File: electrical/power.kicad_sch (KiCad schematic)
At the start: 72 parts

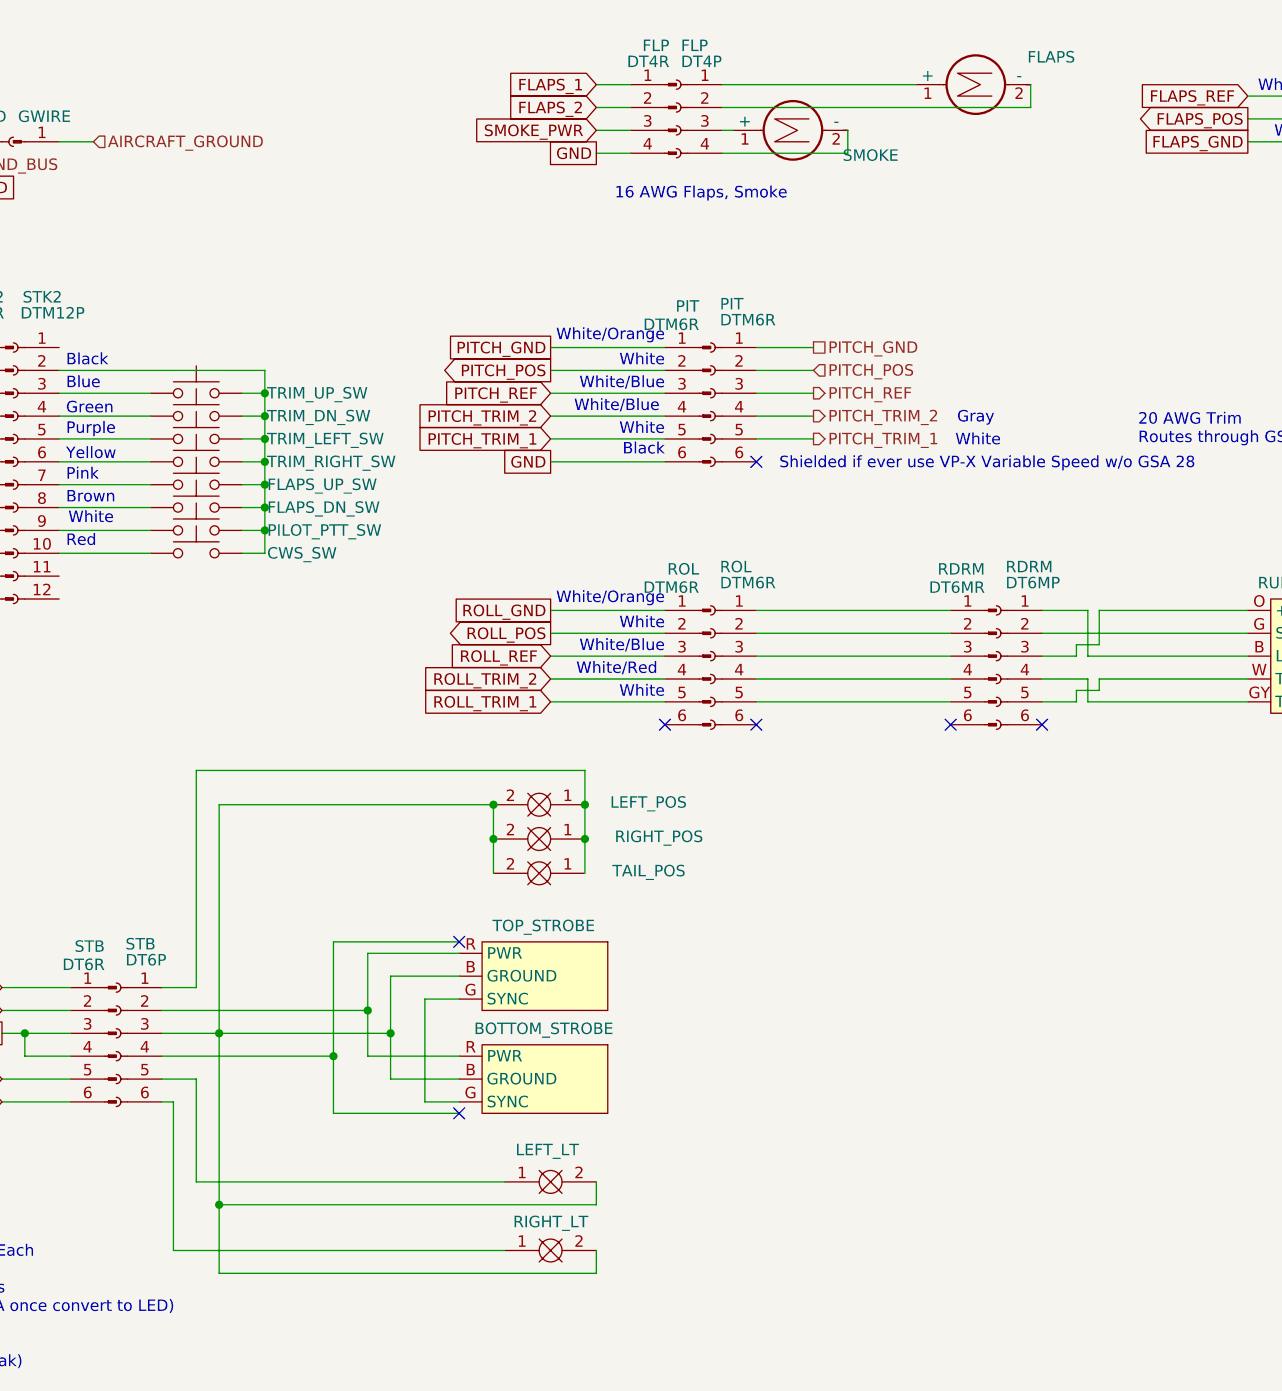
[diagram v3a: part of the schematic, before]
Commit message: Interim check-in getting colors correct.
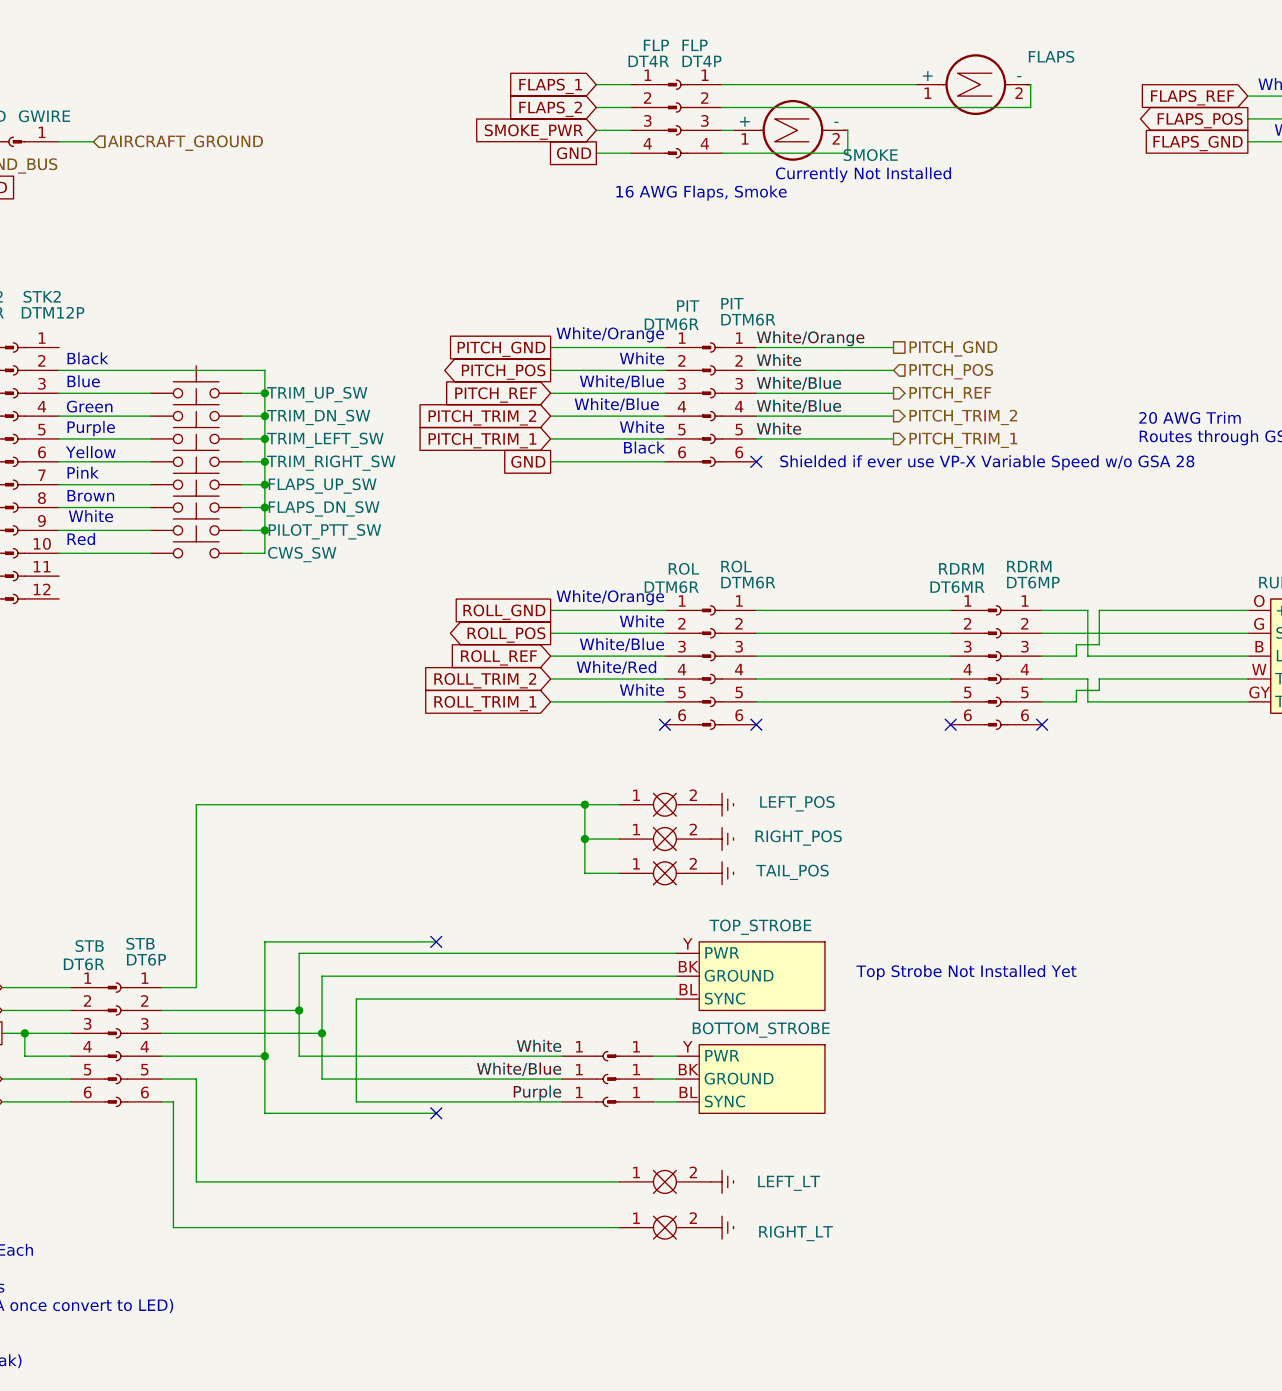
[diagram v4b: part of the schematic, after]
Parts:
- added J1, J4, J5: Conn_01x01_Pin, symbol Connector:Conn_01x01_Pin
- added J2, J3, J6: Conn_01x01_Socket, symbol Connector:Conn_01x01_Socket
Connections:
- net PITCH_TRIM_1 is gone; now on net PITCH_POS: PIT.5 (Pin_5), PIT.5 (Pin_5), VPX.J1_11 (PITCH_TRIM_MOTOR)
- net PITCH_TRIM_2 is gone; now on net PITCH_REF: PIT.4 (Pin_4), PIT.4 (Pin_4), VPX.J1_12 (PITCH_TRIM_MOTOR)
- net PITCH_POS: now also STB.2 (Pin_2), TOP_STROBE.Y (PWR), J2.1 (Pin_1)
- net PITCH_REF: now also STB.3 (Pin_3), TOP_STROBE.BK (GROUND), J3.1 (Pin_1)
- net Earth: now reaches LEFT_LT.2, LEFT_POS.2, RIGHT_LT.2, RIGHT_POS.2, TAIL_POS.2
- net Earth: no longer BOTTOM_STROBE.B (GROUND), STB.3 (Pin_3), TOP_STROBE.B (GROUND)
- new net: BOTTOM_STROBE.BK (GROUND), J4.1 (Pin_1)
- new net: BOTTOM_STROBE.BL (SYNC), J5.1 (Pin_1)
- new net: BOTTOM_STROBE.Y (PWR), J1.1 (Pin_1)
- new net Purple: J6.1 (Pin_1), TOP_STROBE.BL (SYNC)
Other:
- note added: "Currently Not Installed"
- note added: "Top Strobe Not Installed Yet"
- moved on the sheet: BOTTOM_STROBE, LEFT_LT, LEFT_POS, RIGHT_LT, RIGHT_POS, TAIL_POS, TOP_STROBE

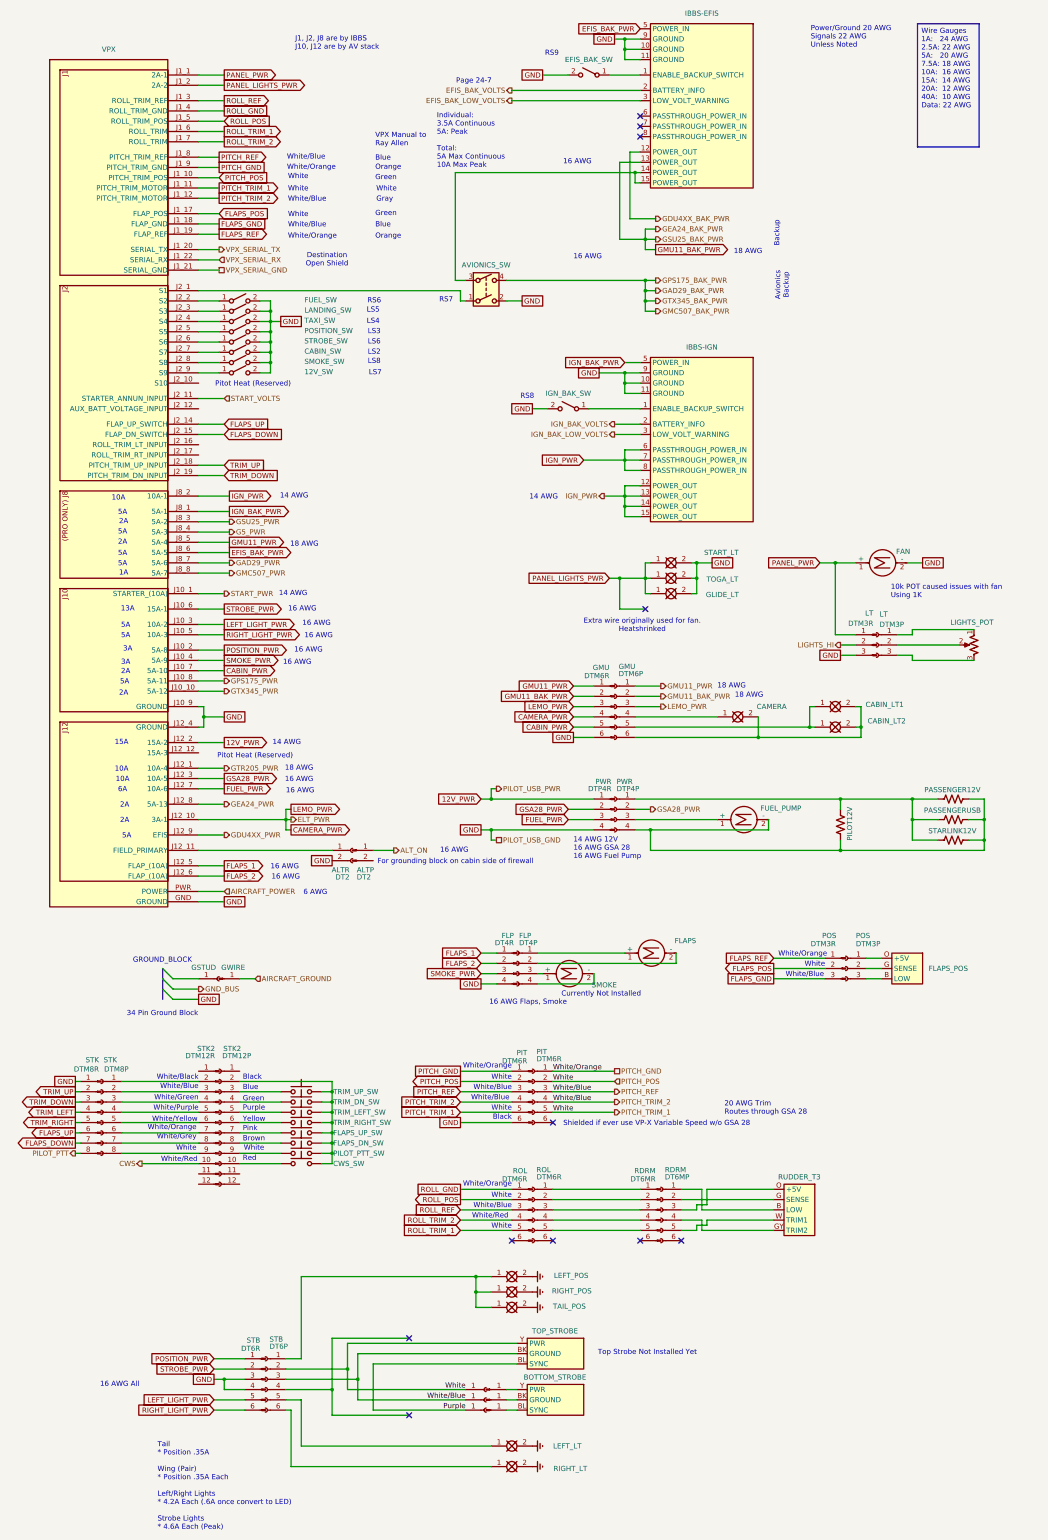
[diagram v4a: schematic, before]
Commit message: Added shielding and wire colors and corrections.
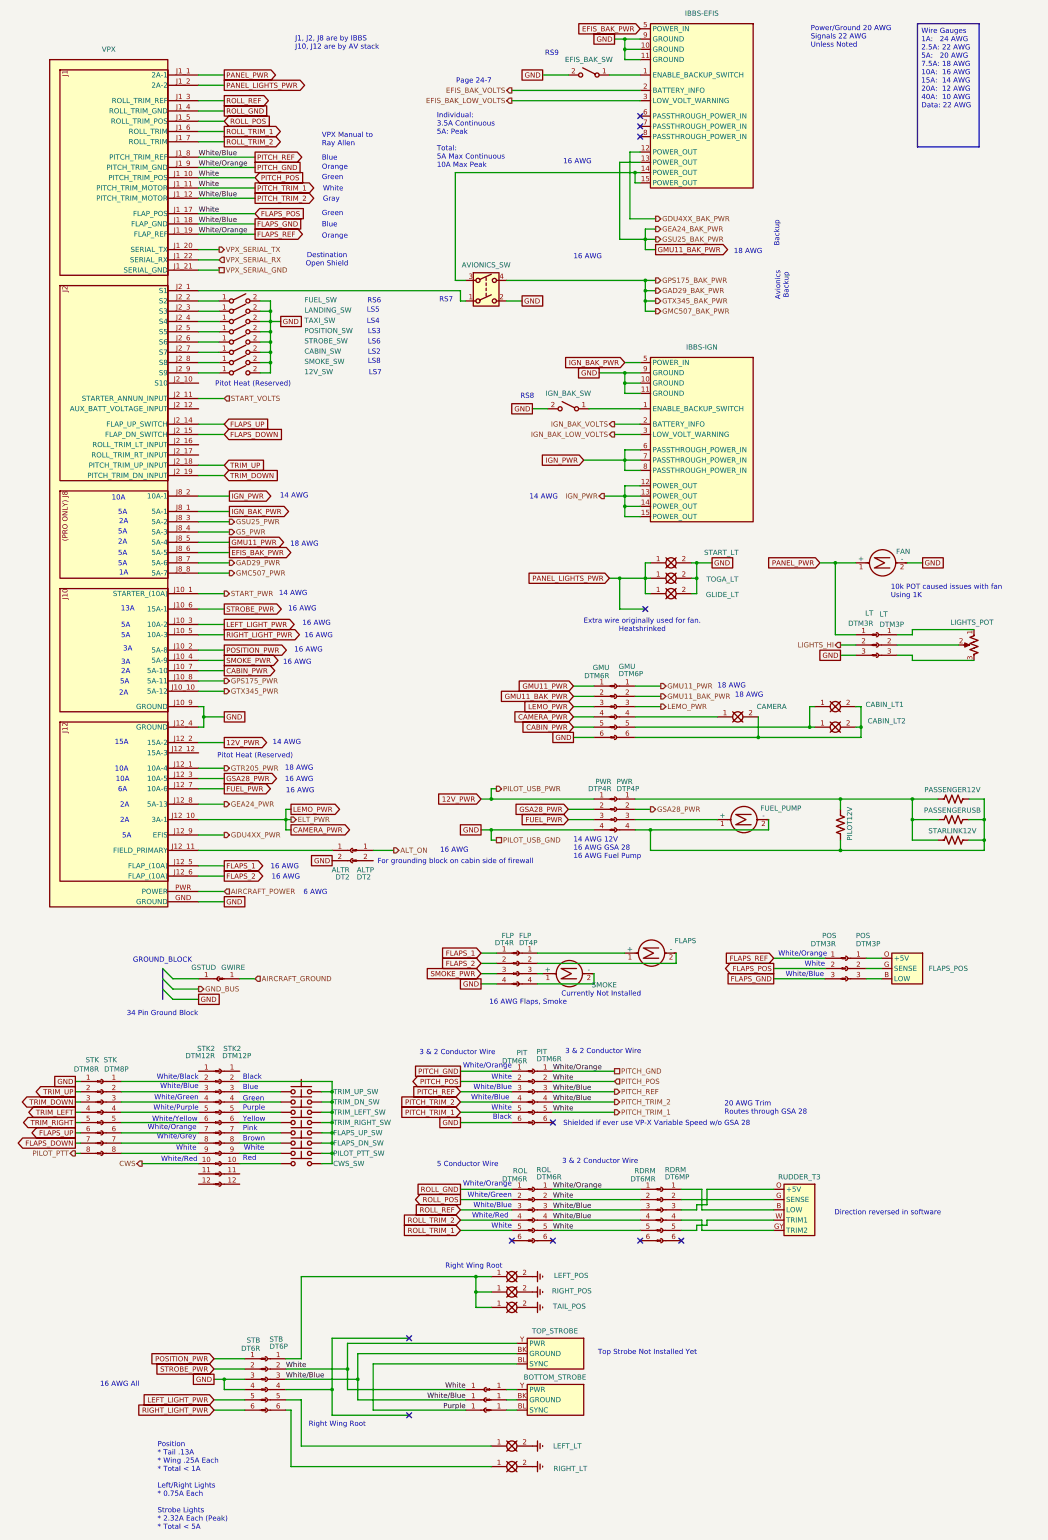
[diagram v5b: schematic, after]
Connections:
- net PITCH_GND is gone; now on net FLAPS_REF: PIT.1 (Pin_1), PIT.1 (Pin_1), VPX.J1_9 (PITCH_TRIM_GND)
- net PITCH_POS is gone; now on net FLAPS_POS: J2.1 (Pin_1), PIT.2 (Pin_2), PIT.2 (Pin_2), PIT.5 (Pin_5), PIT.5 (Pin_5), STB.2 (Pin_2), TOP_STROBE.Y (PWR), VPX.J1_10 (PITCH_TRIM_POS), VPX.J1_11 (PITCH_TRIM_MOTOR)
- net PITCH_REF is gone; now on net FLAPS_GND: J3.1 (Pin_1), PIT.3 (Pin_3), PIT.3 (Pin_3), PIT.4 (Pin_4), PIT.4 (Pin_4), STB.3 (Pin_3), TOP_STROBE.BK (GROUND), VPX.J1_12 (PITCH_TRIM_MOTOR), VPX.J1_8 (PITCH_TRIM_REF)
- net FLAPS_GND: now also RDRM.3 (Pin_3), RDRM.4 (Pin_4), ROL.3 (Pin_3), ROL.4 (Pin_4)
- net FLAPS_POS: now also RDRM.2 (Pin_2), RDRM.5 (Pin_5), ROL.2 (Pin_2), ROL.5 (Pin_5)
- net FLAPS_REF: now also RDRM.1 (Pin_1), ROL.1 (Pin_1)
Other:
- note added: "3 & 2 Conductor Wire"
- note added: "5 Conductor Wire"
- note added: "Direction reversed in software"
- note added: "Position * Tail .13A * Wing .25A Each * Total < 1A Left/Right Lights * 0.75A Each Strobe Lights * 2.32A Each (Peak) * Total < 5A"
- note added: "Right Wing Root"
- note removed: "Tail * Position .35A Wing (Pair) * Position .35A Each Left/Right Lights * 4.2A Each (.6A once convert to LED) Strobe Lights * 4.6A Each (Peak)"

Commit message: Changed Oil Temp to shielded. Added colors that matched what wired.
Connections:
- net Black: now reaches LEFT_POS.1, RIGHT_POS.1, STB.1 (Pin_1), TAIL_POS.1
- net Red: now reaches RIGHT_LT.1, STB.6 (Pin_6)
- net Red: now also LEFT_LT.1, STB.5 (Pin_5)
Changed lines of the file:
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@@
 	(title_block
 		(title "Power Distribution")
-		(date "2025-11-12")
-		(rev "1.2.5")
+		(date "2025-11-13")
+		(rev "1.2.6")
 		(company "N78HR")
 	)
@@
 	(text "Right Wing Root"
 		(exclude_from_sim no)
-		(at 125.222 323.85 0)
+		(at 117.348 322.58 0)
 		(effects
 			(font
@@
 	)
 	(junction
-		(at 125.73 330.2)
-		(diameter 0)
-		(color 0 0 0 0)
-	)
-	(junction
 		(at 90.17 293.37)
 		(diameter 0)
@@
 	)
 	(junction
+		(at 116.84 326.39)
+		(diameter 0)
+		(color 0 0 0 0)
+	)
+	(junction
 		(at 63.5 351.79)
 		(diameter 0)
@@
 	)
 	(junction
-		(at 125.73 326.39)
-		(diameter 0)
-		(color 0 0 0 0)
-	)
-	(junction
 		(at 93.98 349.25)
 		(diameter 0)
@@
 	)
 	(junction
+		(at 116.84 330.2)
+		(diameter 0)
+		(color 0 0 0 0)
+	)
+	(junction
 		(at 167.64 82.55)
 		(diameter 0)
@@
 	(wire
 		(pts
-			(xy 125.73 330.2) (xy 125.73 326.39)
+			(xy 116.84 330.2) (xy 116.84 326.39)
 		)
 		(stroke
@@
 	(wire
 		(pts
-			(xy 125.73 334.01) (xy 125.73 330.2)
+			(xy 116.84 334.01) (xy 116.84 330.2)
 		)
 		(stroke
@@
 	(wire
 		(pts
-			(xy 125.73 326.39) (xy 129.54 326.39)
-		)
-		(stroke
-			(width 0)
-			(type default)
-		)
-	)
-	(wire
-		(pts
 			(xy 167.64 82.55) (xy 170.18 82.55)
 		)
@@
 	(wire
 		(pts
-			(xy 129.54 330.2) (xy 125.73 330.2)
-		)
-		(stroke
-			(width 0)
-			(type default)
-		)
-	)
-	(wire
-		(pts
 			(xy 247.65 213.36) (xy 251.46 213.36)
 		)
@@
 	(wire
 		(pts
+			(xy 116.84 330.2) (xy 129.54 330.2)
+		)
+		(stroke
+			(width 0)
+			(type default)
+		)
+	)
+	(wire
+		(pts
 			(xy 133.35 356.87) (xy 135.89 356.87)
 		)
@@
 	(wire
 		(pts
-			(xy 129.54 334.01) (xy 125.73 334.01)
+			(xy 129.54 334.01) (xy 116.84 334.01)
 		)
 		(stroke
@@
 	(wire
 		(pts
+			(xy 116.84 326.39) (xy 129.54 326.39)
+		)
+		(stroke
+			(width 0)
+			(type default)
+		)
+	)
+	(wire
+		(pts
 			(xy 154.94 254) (xy 154.94 251.46)
 		)
@@
 	(wire
 		(pts
-			(xy 82.55 326.39) (xy 125.73 326.39)
+			(xy 82.55 326.39) (xy 116.84 326.39)
 		)
 		(stroke
@@
 		)
 	)
+	(label "Red"
+		(at 83.82 368.3 0)
+		(effects
+			(font
+				(size 1.27 1.27)
+			)
+			(justify left bottom)
+		)
+	)
 	(label "White"
 		(at 144.78 307.34 0)
@@
 		)
 	)
+	(label "Black"
+		(at 129.54 326.39 180)
+		(effects
+			(font
+				(size 1.27 1.27)
+			)
+			(justify right bottom)
+		)
+	)
 	(label "White{slash}Blue"
 		(at 144.78 309.88 0)
@@
 		)
 	)
+	(label "Red"
+		(at 83.82 373.38 0)
+		(effects
+			(font
+				(size 1.27 1.27)
+			)
+			(justify left bottom)
+		)
+	)
 	(label "White{slash}Blue"
 		(at 78.74 351.79 0)
@@
 		)
 	)
+	(label "Black"
+		(at 129.54 330.2 180)
+		(effects
+			(font
+				(size 1.27 1.27)
+			)
+			(justify right bottom)
+		)
+	)
